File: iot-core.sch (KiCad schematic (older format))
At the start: 49 parts, among them P1 USB, P10 CONN_01X01, P11 CONN_01X01, P2 CONN_01X02, P3 CONN_01X16, P4 CONN_01X04, P5 CONN_01X16, P6 CONN_01X03, P7 CONN_01X03, P8 CONN_01X01, P9 CONN_01X01, SW1 RST, SW2 SW_PUSH_SMALL_H, U1 LP2985LV, U2 STM32F103C8Tx, U3 ESP-07v2, Y1 8MHz

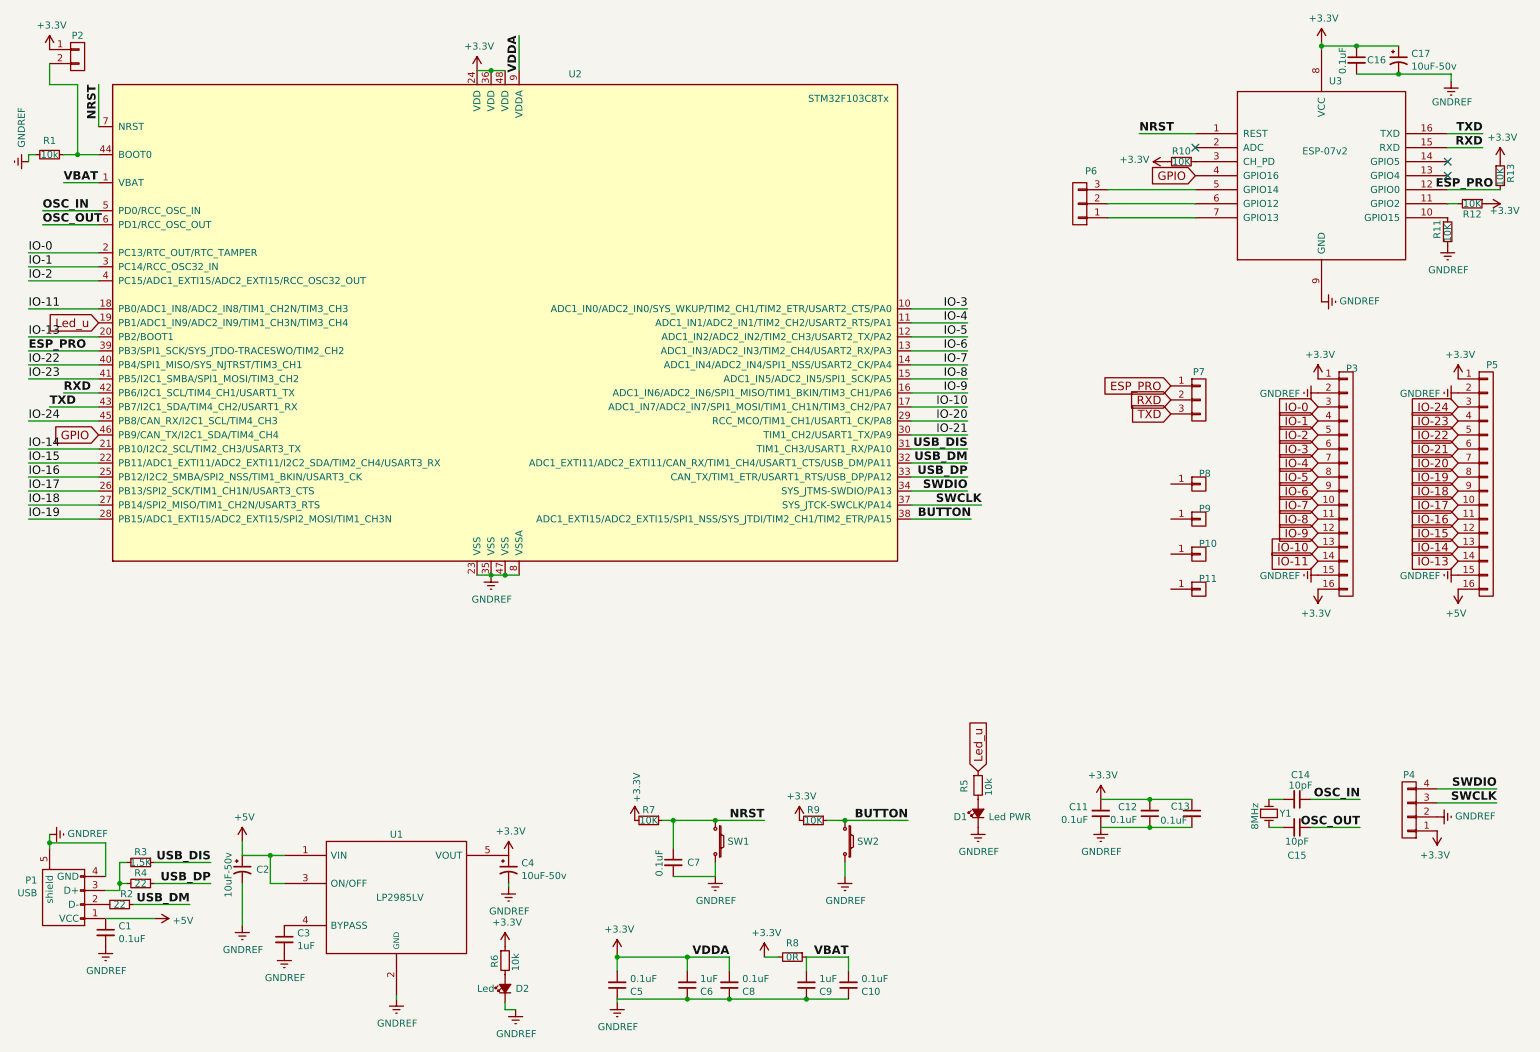
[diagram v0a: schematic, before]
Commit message: Fix DAO DONG THACH ANH KHONG NOI GND, pin ESP_PRO to PB0, GPIO16 to PB11,DELETE header BOOT 0
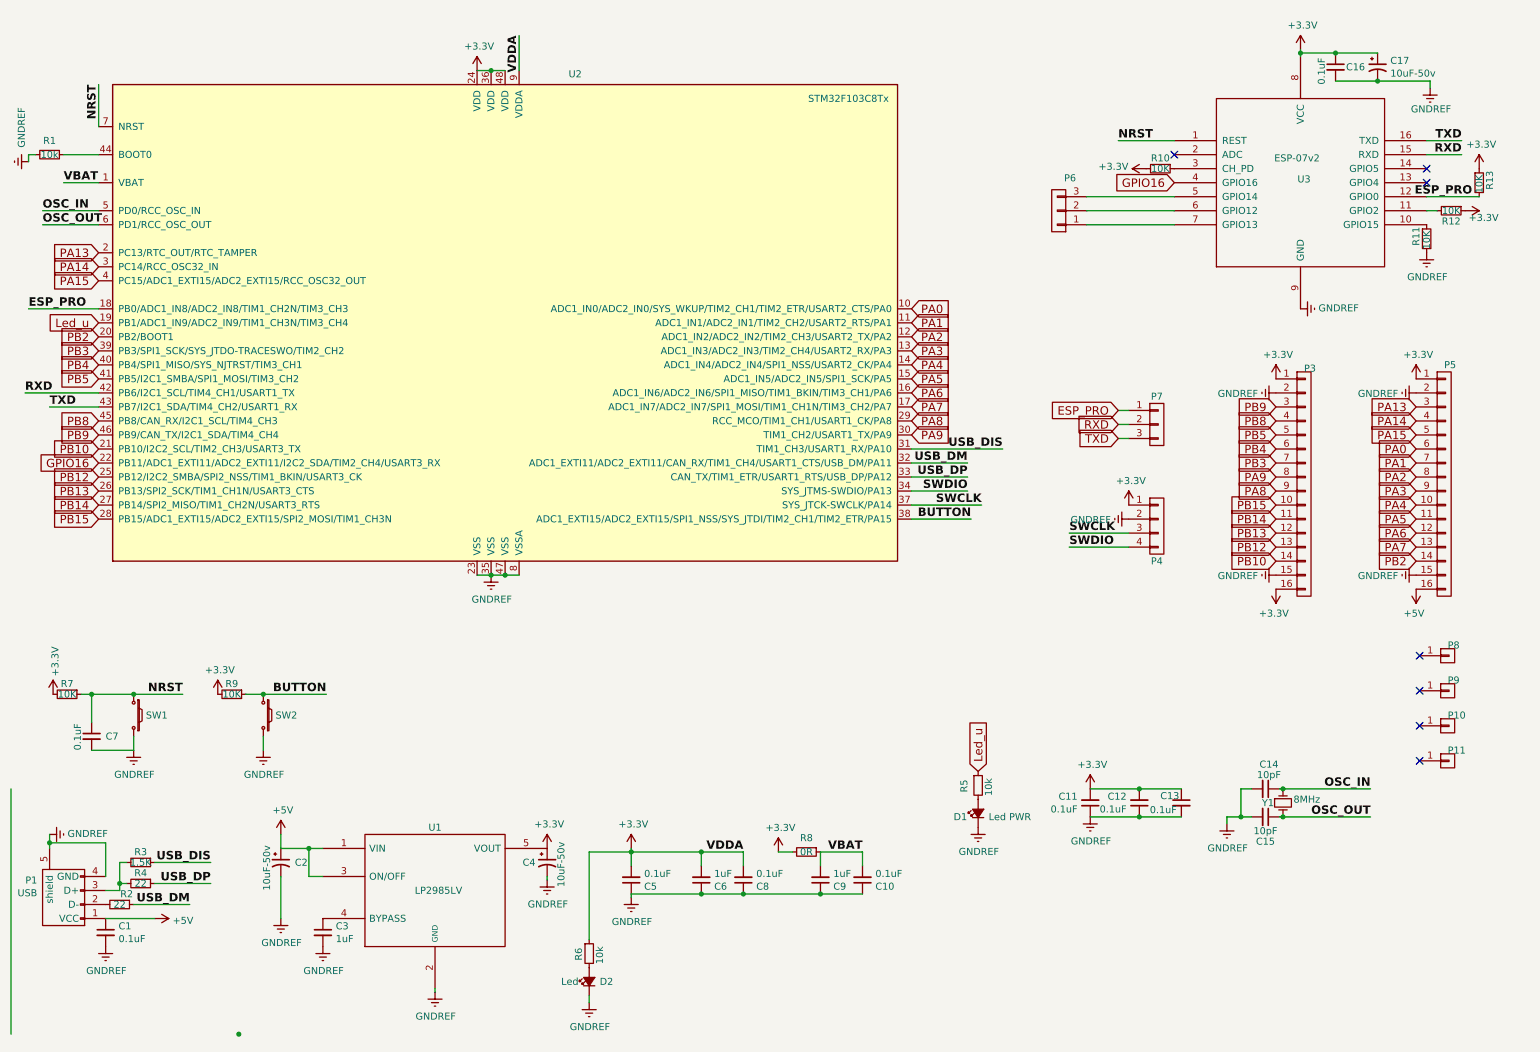
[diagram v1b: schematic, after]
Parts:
- removed P2: CONN_01X02, Pin_Headers:Pin_Header_Straight_1x02, symbol CONN_01X02
- Y1: footprint crystal:crystal-HC49UP -> Crystal:HC49_sm
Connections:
- net ESP_PRO: now also U2.18 (PB0/ADC1_IN8/ADC2_IN8/TIM1_CH2N/TIM3_CH3); no longer U2.39 (PB3/SPI1_SCK/SYS_JTDO-TRACESWO/TIM2_CH2)
- net GNDREF: now also C14.2, C15.2
- net OSC_IN: now also Y1.1
- net OSC_OUT: now also Y1.2
- net GPIO renamed GPIO16
- net GPIO16: now also U2.22 (PB11/ADC1_EXTI11/ADC2_EXTI11/I2C2_SDA/TIM2_CH4/USART3_RX); no longer U2.46 (PB9/CAN_TX/I2C1_SDA/TIM4_CH4)
- net IO-0 renamed PA13
- net PA13: now also P5.3 (P3); no longer P3.3 (P3)
- net IO-1 renamed PA14
- net PA14: now also P5.4 (P4); no longer P3.4 (P4)
- net IO-10 renamed PA7
- net PA7: now also P5.13 (P13); no longer P3.13 (P13)
- net IO-11 renamed PB10
- net PB10: now also U2.21 (PB10/I2C2_SCL/TIM2_CH3/USART3_TX); no longer U2.18 (PB0/ADC1_IN8/ADC2_IN8/TIM1_CH2N/TIM3_CH3)
- net IO-13 renamed PB2
- removed net IO-14: P5.13 (P13), U2.21 (PB10/I2C2_SCL/TIM2_CH3/USART3_TX)
- net IO-15 renamed PA6
- net PA6: now also U2.16 (ADC1_IN6/ADC2_IN6/SPI1_MISO/TIM1_BKIN/TIM3_CH1/PA6); no longer U2.22 (PB11/ADC1_EXTI11/ADC2_EXTI11/I2C2_SDA/TIM2_CH4/USART3_RX)
- net IO-16 renamed PA5
- net PA5: now also U2.15 (ADC1_IN5/ADC2_IN5/SPI1_SCK/PA5); no longer U2.25 (PB12/I2C2_SMBA/SPI2_NSS/TIM1_BKIN/USART3_CK)
- net IO-17 renamed PA4
- net PA4: now also U2.14 (ADC1_IN4/ADC2_IN4/SPI1_NSS/USART2_CK/PA4); no longer U2.26 (PB13/SPI2_SCK/TIM1_CH1N/USART3_CTS)
- net IO-18 renamed PA3
- net PA3: now also U2.13 (ADC1_IN3/ADC2_IN3/TIM2_CH4/USART2_RX/PA3); no longer U2.27 (PB14/SPI2_MISO/TIM1_CH2N/USART3_RTS)
- net IO-19 renamed PA2
- net PA2: now also U2.12 (ADC1_IN2/ADC2_IN2/TIM2_CH3/USART2_TX/PA2); no longer U2.28 (PB15/ADC1_EXTI15/ADC2_EXTI15/SPI2_MOSI/TIM1_CH3N)
- net IO-2 renamed PA15
- net PA15: now also P5.5 (P5); no longer P3.5 (P5)
- net IO-20 renamed PA1
- net PA1: now also U2.11 (ADC1_IN1/ADC2_IN1/TIM2_CH2/USART2_RTS/PA1); no longer U2.29 (RCC_MCO/TIM1_CH1/USART1_CK/PA8)
- net IO-21 renamed PA0
- net PA0: now also U2.10 (ADC1_IN0/ADC2_IN0/SYS_WKUP/TIM2_CH1/TIM2_ETR/USART2_CTS/PA0); no longer U2.30 (TIM1_CH2/USART1_TX/PA9)
- net IO-22 renamed PB4
- net PB4: now also P3.6 (P6); no longer P5.5 (P5)
- net IO-23 renamed PB5
- net PB5: now also P3.5 (P5); no longer P5.4 (P4)
- net IO-24 renamed PB8
- net PB8: now also P3.4 (P4); no longer P5.3 (P3)
- removed net IO-3: P3.6 (P6), U2.10 (ADC1_IN0/ADC2_IN0/SYS_WKUP/TIM2_CH1/TIM2_ETR/USART2_CTS/PA0)
- net IO-4 renamed PB3
- net PB3: now also U2.39 (PB3/SPI1_SCK/SYS_JTDO-TRACESWO/TIM2_CH2); no longer U2.11 (ADC1_IN1/ADC2_IN1/TIM2_CH2/USART2_RTS/PA1)
- net IO-5 renamed PA9
- net PA9: now also U2.30 (TIM1_CH2/USART1_TX/PA9); no longer U2.12 (ADC1_IN2/ADC2_IN2/TIM2_CH3/USART2_TX/PA2)
- net IO-6 renamed PA8
- net PA8: now also U2.29 (RCC_MCO/TIM1_CH1/USART1_CK/PA8); no longer U2.13 (ADC1_IN3/ADC2_IN3/TIM2_CH4/USART2_RX/PA3)
- net IO-7 renamed PB15
- net PB15: now also U2.28 (PB15/ADC1_EXTI15/ADC2_EXTI15/SPI2_MOSI/TIM1_CH3N); no longer U2.14 (ADC1_IN4/ADC2_IN4/SPI1_NSS/USART2_CK/PA4)
- net IO-8 renamed PB14
- net PB14: now also U2.27 (PB14/SPI2_MISO/TIM1_CH2N/USART3_RTS); no longer U2.15 (ADC1_IN5/ADC2_IN5/SPI1_SCK/PA5)
- net IO-9 renamed PB13
- net PB13: now also U2.26 (PB13/SPI2_SCK/TIM1_CH1N/USART3_CTS); no longer U2.16 (ADC1_IN6/ADC2_IN6/SPI1_MISO/TIM1_BKIN/TIM3_CH1/PA6)
- new net PB12: P3.13 (P13), U2.25 (PB12/I2C2_SMBA/SPI2_NSS/TIM1_BKIN/USART3_CK)
- new net PB9: P3.3 (P3), U2.46 (PB9/CAN_TX/I2C1_SDA/TIM4_CH4)
- no-connect marks 3 -> 7
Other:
- moved on the sheet: C10, C11, C12, C13, C14, C15, C16, C17, C2, C3, C4, C5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

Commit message: Add sub Englishon README file
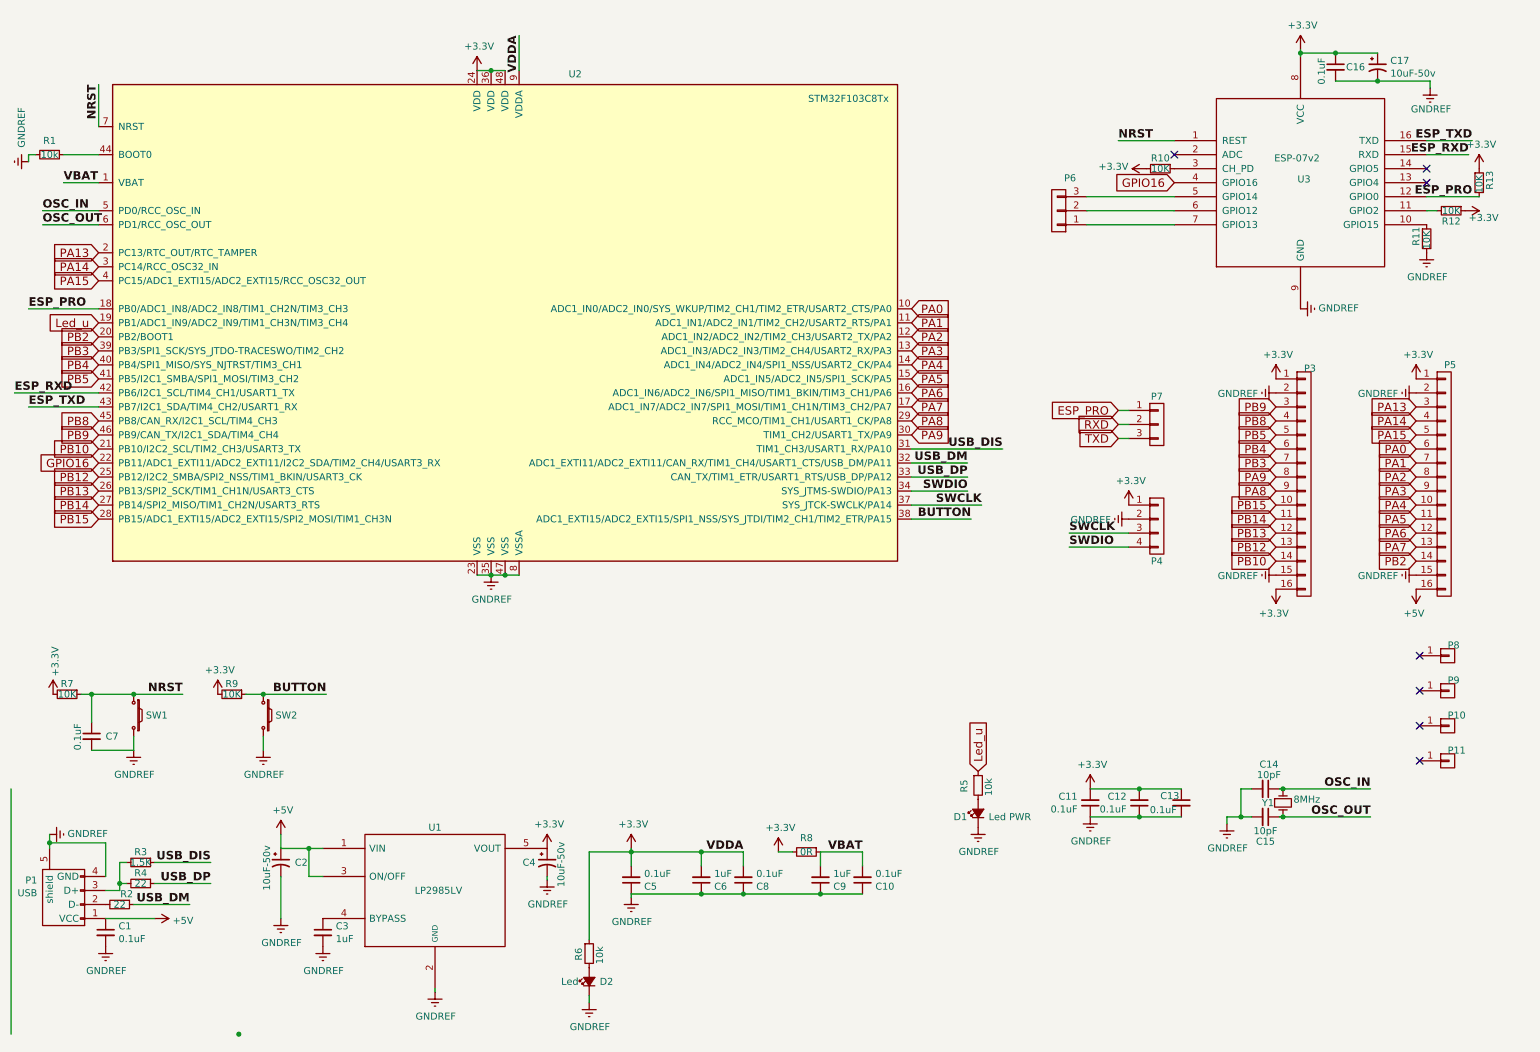
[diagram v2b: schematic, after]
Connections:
- net RXD: no longer U2.42 (PB6/I2C1_SCL/TIM4_CH1/USART1_TX), U3.15 (RXD)
- net TXD: no longer U2.43 (PB7/I2C1_SDA/TIM4_CH2/USART1_RX), U3.16 (TXD)
- new net ESP_RXD: U2.42 (PB6/I2C1_SCL/TIM4_CH1/USART1_TX), U3.15 (RXD)
- new net ESP_TXD: U2.43 (PB7/I2C1_SDA/TIM4_CH2/USART1_RX), U3.16 (TXD)
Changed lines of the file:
@@
 	1    0    0    -1
 $EndComp
-Text Label 10825 1400 2    60   ~ 12
-TXD
-Text Label 10825 1500 2    60   ~ 12
-RXD
+Text Label 10900 1400 2    60   ~ 12
+ESP_TXD
+Text Label 10875 1500 2    60   ~ 12
+ESP_RXD
 NoConn ~ 10575 1600
 NoConn ~ 10575 1700
@@
 	0    1    1    0
 $EndComp
-Text Label 750  3300 0    60   ~ 12
-TXD
-Text Label 575  3200 0    60   ~ 12
-RXD
+Text Label 600  3300 0    60   ~ 12
+ESP_TXD
+Text Label 500  3200 0    60   ~ 12
+ESP_RXD
 $Comp
 L +3.3V #PWR027
@@
 Connection ~ 9675 775
 Wire Wire Line
-	10575 1400 10825 1400
-Wire Wire Line
-	10575 1500 10825 1500
-Wire Wire Line
-	1100 3300 750  3300
+	10575 1400 10900 1400
+Wire Wire Line
+	10575 1500 10875 1500
+Wire Wire Line
+	600  3300 1100 3300
 Wire Wire Line
 	6900 4000 7400 4000
@@
 	10650 1900 10575 1900
 Wire Wire Line
-	575  3200 1100 3200
+	500  3200 1100 3200
 Wire Wire Line
 	3800 4500 4100 4500
